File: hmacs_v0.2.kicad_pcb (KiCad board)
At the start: 2 copper layers, 70 x 115 mm, 23 parts, among them J1 EXT_CONNECTOR, J2 MODULE_CONN_2, J3 SENSE_PIN_CONNECTOR, J4 MODULE_CONN_1, J5 AC_INPUT, J6 RFID_HEADER, J7 RELAY_CONNECTOR, J8 SSR_CONNECTOR, Q1 RELAY_SIG_PNP_EBC

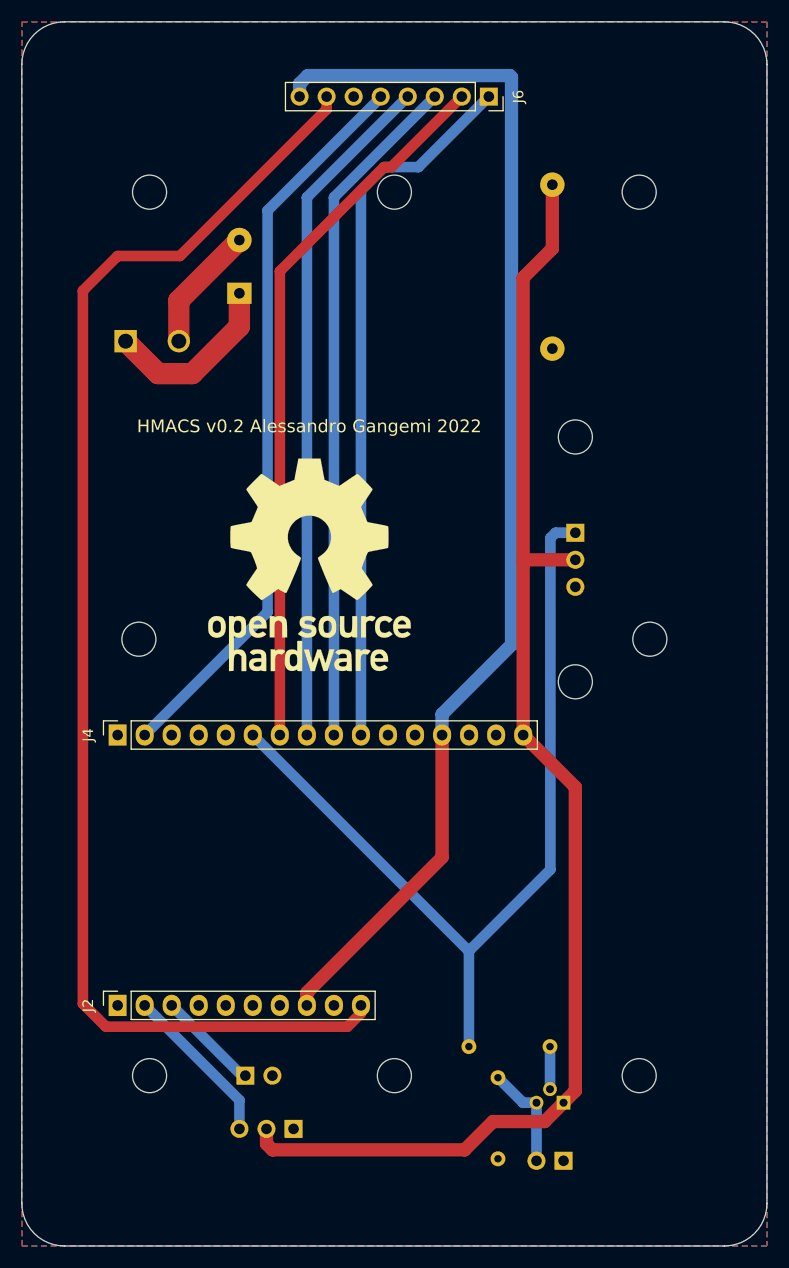
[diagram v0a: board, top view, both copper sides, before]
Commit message: Fix board errors and bump version to 0.3.0
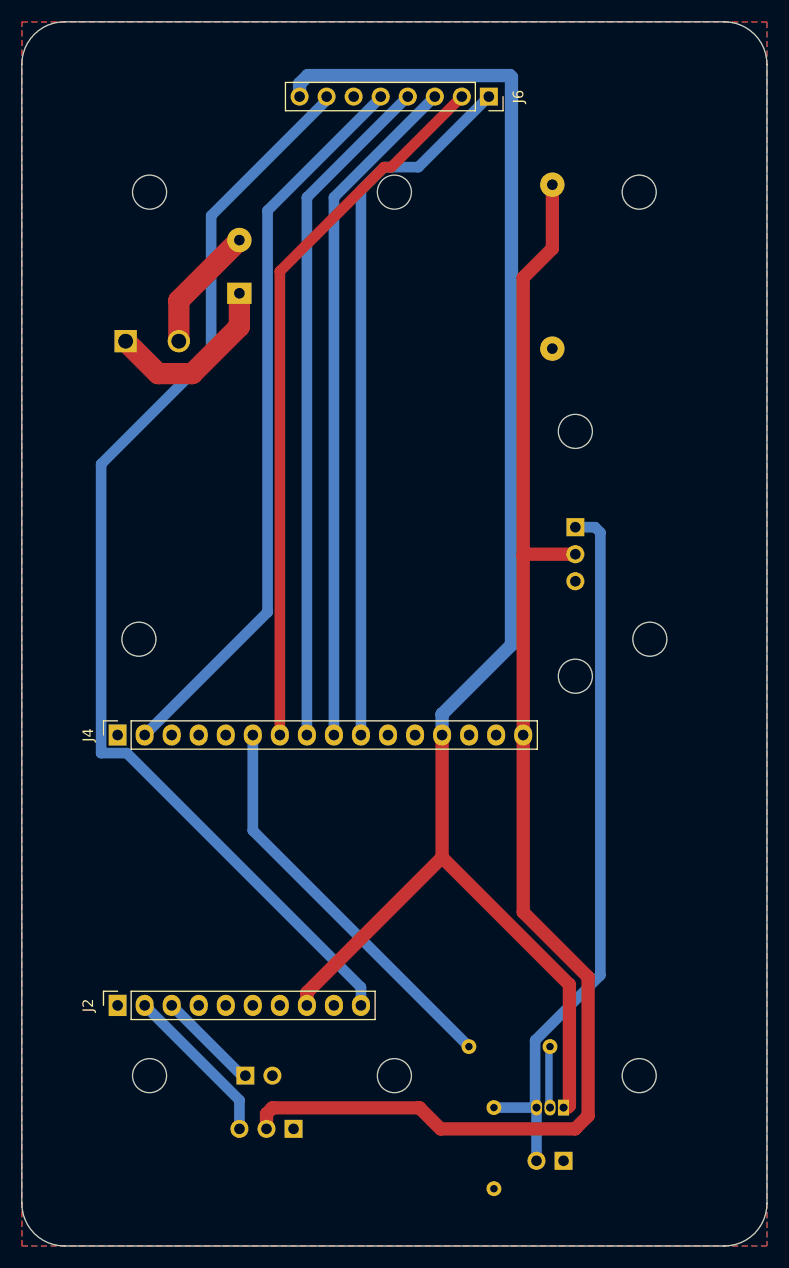
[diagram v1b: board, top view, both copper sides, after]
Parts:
- Q1: value RELAY_SIG_PNP_EBC -> 2N3906; footprint Package_TO_SOT_THT:TO-92 -> Package_TO_SOT_THT:TO-92_Inline
- REF**: value OSHW-Logo_19x20mm_SilkScreen -> OSHW-Logo_11.4x12mm_SilkScreen; footprint Symbol:OSHW-Logo_19x20mm_SilkScreen -> Symbol:OSHW-Logo_11.4x12mm_SilkScreen; moved to B.Cu
- moved REF** 36.8 mm to (103.0, 112.0), turned to 180 degrees
- moved R2 2.84 mm to (94.3, 137.0)
- moved J7 0.53 mm to (102.0, 82.5)
- moved REF** 0.53 mm to (102.0, 96.5)
- moved REF** 0.53 mm to (102.0, 73.5)
- moved Q1 0.46 mm to (100.9, 137.0)
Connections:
- J4 pad 6: RELAY -> RELAY_SIG
- J8 pad 2: SSR -> RELAY
- Q1 pad 1: +5V -> +3V3
- Q1 pad 3: SSR -> RELAY
- R1 pad 1: RELAY -> RELAY_SIG
- R2 pad 1: SSR -> RELAY
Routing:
- net RELAY_SIG: track 0.00 -> 37.7 mm
- net +3V3: track 116.6 -> 145.2 mm
- net RESET: track 126.4 -> 105.7 mm
- net RELAY: track 82.2 -> 68.2 mm
- net SSR: track 10.1 -> 0.00 mm
- net +5V: track 126.2 -> 129.3 mm
- net Net-(Q1-Pad2): track 3.62 -> 5.77 mm
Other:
- board text added: "D0/GPIO16-IRQ D1/GPIO5-SCL D2/GPIO4-SCA D4/GPIO2-RELAY_SIG D5/GPIO14-SCK D6/GPIO12-MISO D7/GPIO13-MOSI D8/GPIO15-SDA SD2/GPIO9-SENSE SD3/GPIO10-CARD_PRESENT"
- board text added: "HMACS v0.3.0 Alessandro Gangemi 2022 Hammonton Makers"
- board text added: "SENSE"
- board text removed: "D0/GPIO16-IRQ D1/GPIO5-SCL D2/GPIO4-SCA D4/GPIO2-RELAY D5/GPIO14-SCK D6/GPIO12-MISO D7/GPIO13-MOSI D8/GPIO15-SDA SD2/GPIO9-SENSE SD3/GPIO10-CARD_PRESENT"
- board text removed: "HMACS v0.2 Alessandro Gangemi 2022"

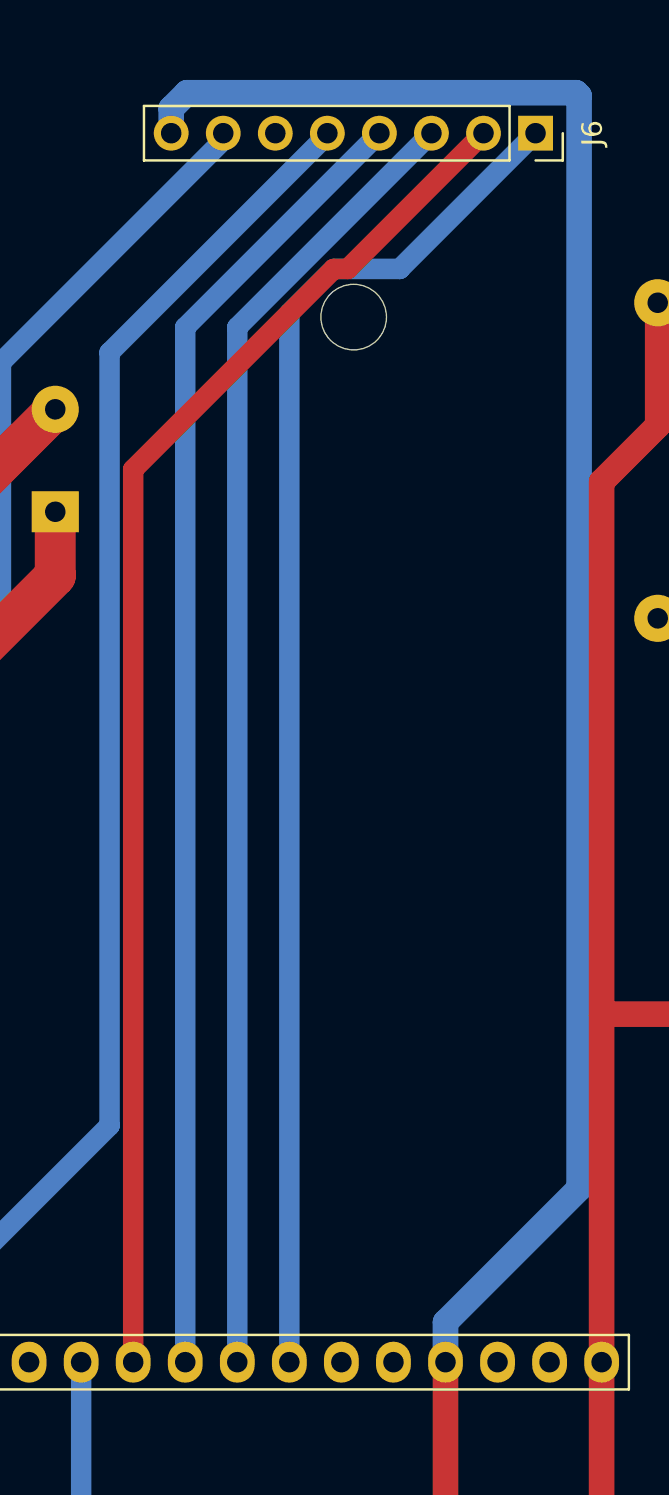
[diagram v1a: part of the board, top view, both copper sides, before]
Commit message: Remove mounting hole under the AC/DC converter
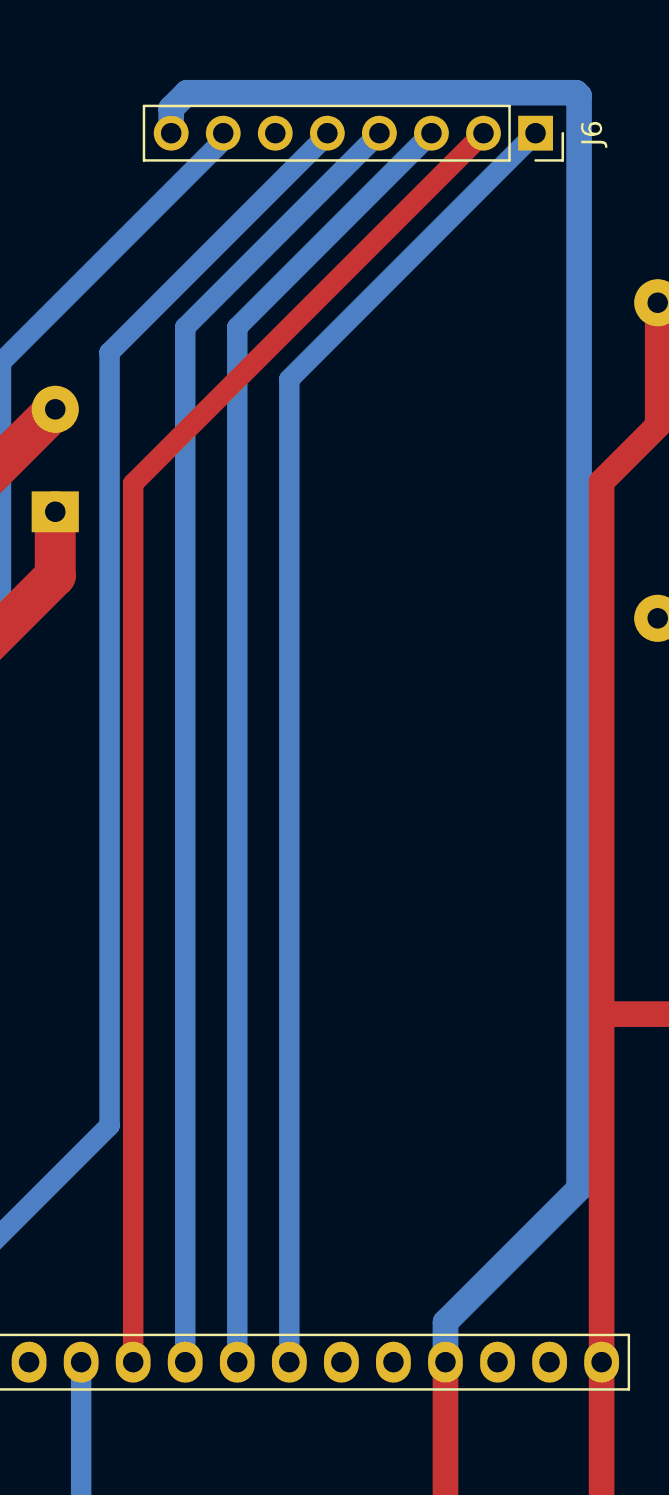
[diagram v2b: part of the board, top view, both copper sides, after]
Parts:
- removed the REF** at (85.0, 51.0)
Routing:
- net SDA: track 66.8 -> 65.0 mm
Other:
- rule pad_to_mask_clearance: 0 -> 0.0508
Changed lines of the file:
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@@
       (dielectric_constraints no)
     )
-    (pad_to_mask_clearance 0)
+    (pad_to_mask_clearance 0.0508)
     (aux_axis_origin 50 150)
     (pcbplotparams
@@
   (footprint "MountingHole:MountingHole_3.2mm_M3" (layer "F.Cu")
     (at 109 93)
-    (descr "Mounting Hole 3.2mm, no annular, M3")
-    (tags "mounting hole 3.2mm no annular m3")
-    (attr exclude_from_pos_files exclude_from_bom)
-    (fp_text reference "REF**" (at 0 -4.2) (layer "F.SilkS") hide
-      (effects (font (size 1 1) (thickness 0.15)))
-    )
-    (fp_text value "MountingHole_3.2mm_M3" (at 0 4.2) (layer "F.Fab")
-      (effects (font (size 1 1) (thickness 0.15)))
-    )
-    (fp_text user "${REFERENCE}" (at 0 0) (layer "F.Fab")
-      (effects (font (size 1 1) (thickness 0.15)))
-    )
-    (fp_circle (center 0 0) (end 3.2 0) (layer "Cmts.User") (width 0.15) (fill none))
-    (fp_circle (center 0 0) (end 3.45 0) (layer "F.CrtYd") (width 0.05) (fill none))
-    (pad "" np_thru_hole circle (at 0 0) (size 3.2 3.2) (drill 3.2) (layers *.Cu *.Mask))
-  )
-  (footprint "MountingHole:MountingHole_3.2mm_M3" (layer "F.Cu")
-    (at 85 51)
     (descr "Mounting Hole 3.2mm, no annular, M3")
     (tags "mounting hole 3.2mm no annular m3")
@@
   (segment (start 98.35 137) (end 98.220489 136.870489) (width 1) (layer "B.Cu") (net 14))
   (segment (start 98.35 137) (end 98.35 142) (width 1) (layer "B.Cu") (net 14))
-  (segment (start 74.24 58.437274) (end 74.24 102) (width 1) (layer "F.Cu") (net 15))
-  (segment (start 84.709521 48.650479) (end 84.026795 48.650479) (width 1) (layer "F.Cu") (net 15))
-  (segment (start 84.026795 48.650479) (end 74.24 58.437274) (width 1) (layer "F.Cu") (net 15))
-  (segment (start 91.335 42.025) (end 84.709521 48.650479) (width 1) (layer "F.Cu") (net 15))
+  (segment (start 74.24 59.12) (end 91.335 42.025) (width 1) (layer "F.Cu") (net 15))
+  (segment (start 74.24 102) (end 74.24 59.12) (width 1) (layer "F.Cu") (net 15))
   (segment (start 76.78 102) (end 76.78 51.5) (width 1) (layer "B.Cu") (net 16))
   (segment (start 76.78 51.5) (end 86.255 42.025) (width 1) (layer "B.Cu") (net 16))
   (segment (start 79.32 102) (end 79.32 51.5) (width 1) (layer "B.Cu") (net 17))
   (segment (start 79.32 51.5) (end 88.795 42.025) (width 1) (layer "B.Cu") (net 17))
-  (segment (start 81.86 102) (end 81.86 50.817274) (width 1) (layer "B.Cu") (net 18))
-  (segment (start 81.86 50.817274) (end 84.026795 48.650479) (width 1) (layer "B.Cu") (net 18))
-  (segment (start 84.026795 48.650479) (end 87.249521 48.650479) (width 1) (layer "B.Cu") (net 18))
-  (segment (start 87.249521 48.650479) (end 93.875 42.025) (width 1) (layer "B.Cu") (net 18))
+  (segment (start 81.86 54.04) (end 93.875 42.025) (width 1) (layer "B.Cu") (net 18))
+  (segment (start 81.86 102) (end 81.86 54.04) (width 1) (layer "B.Cu") (net 18))
   (segment (start 97.1 102) (end 97.1 85.1) (width 1.25) (layer "F.Cu") (net 21))
   (segment (start 73.550489 137.025489) (end 87.36524 137.025489) (width 1.25) (layer "F.Cu") (net 21))
